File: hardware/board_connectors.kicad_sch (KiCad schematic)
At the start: 15 parts, among them J1 AudioJack2_Ground, J1 Conn_02x10_Odd_Even, J2 Conn_02x10_Odd_Even, J3 Conn_02x10_Odd_Even, J5 AudioJack2_Ground, J6 Conn_02x03_Odd_Even, J7 AudioJack2_Ground, J7 USB_B_Micro

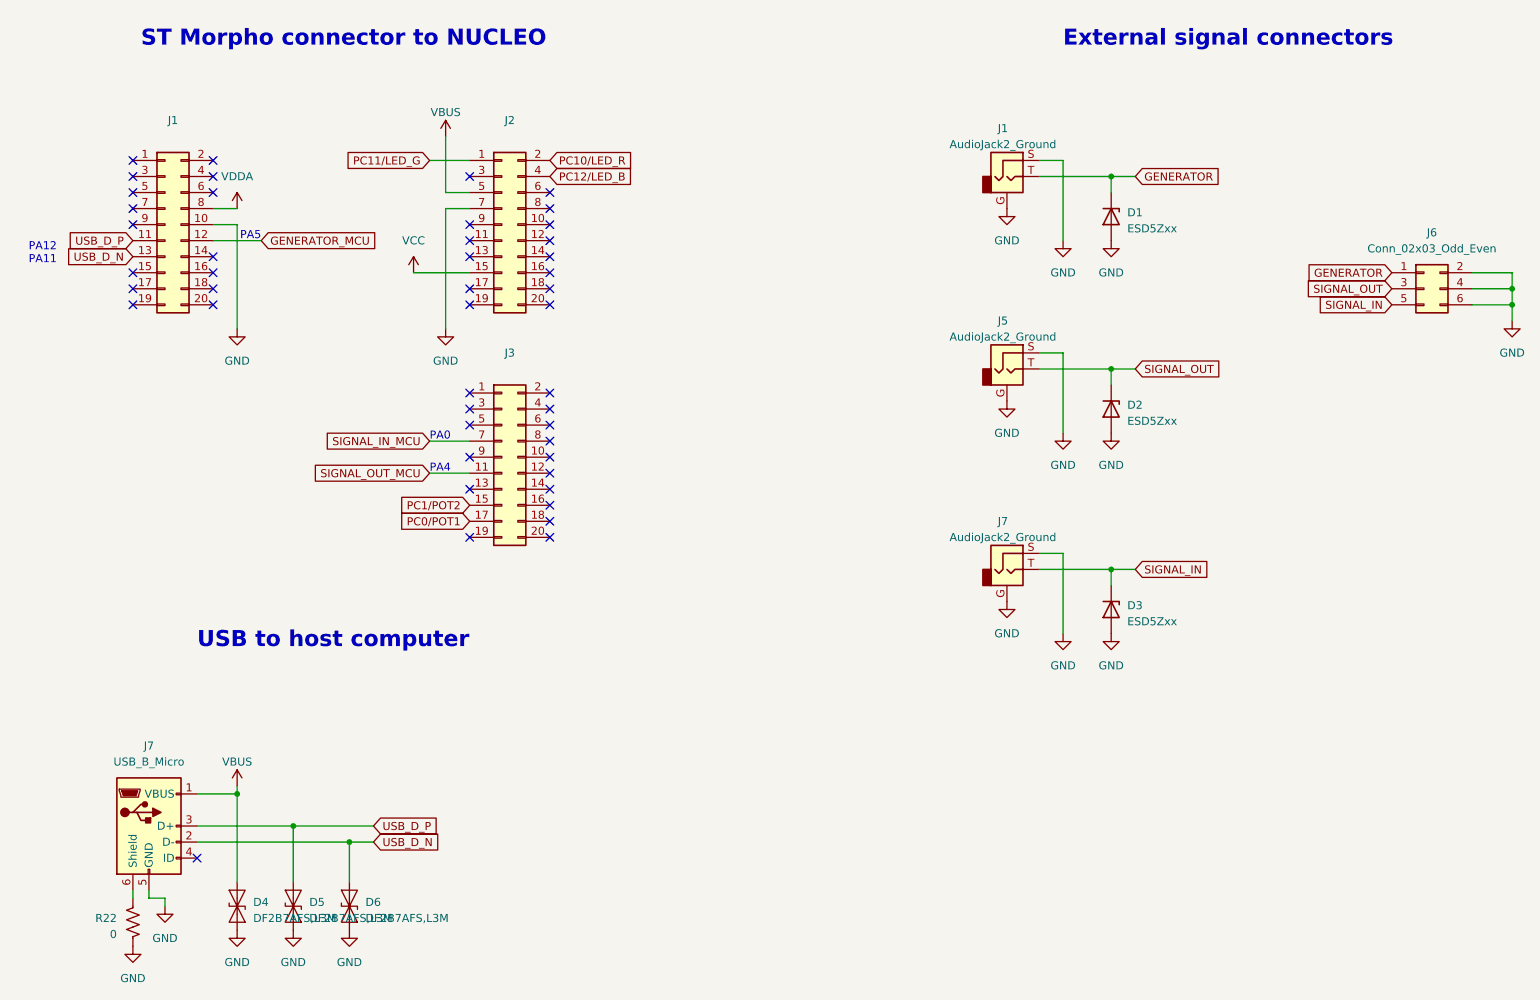
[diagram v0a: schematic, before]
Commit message: finalize pcb design; add layout file
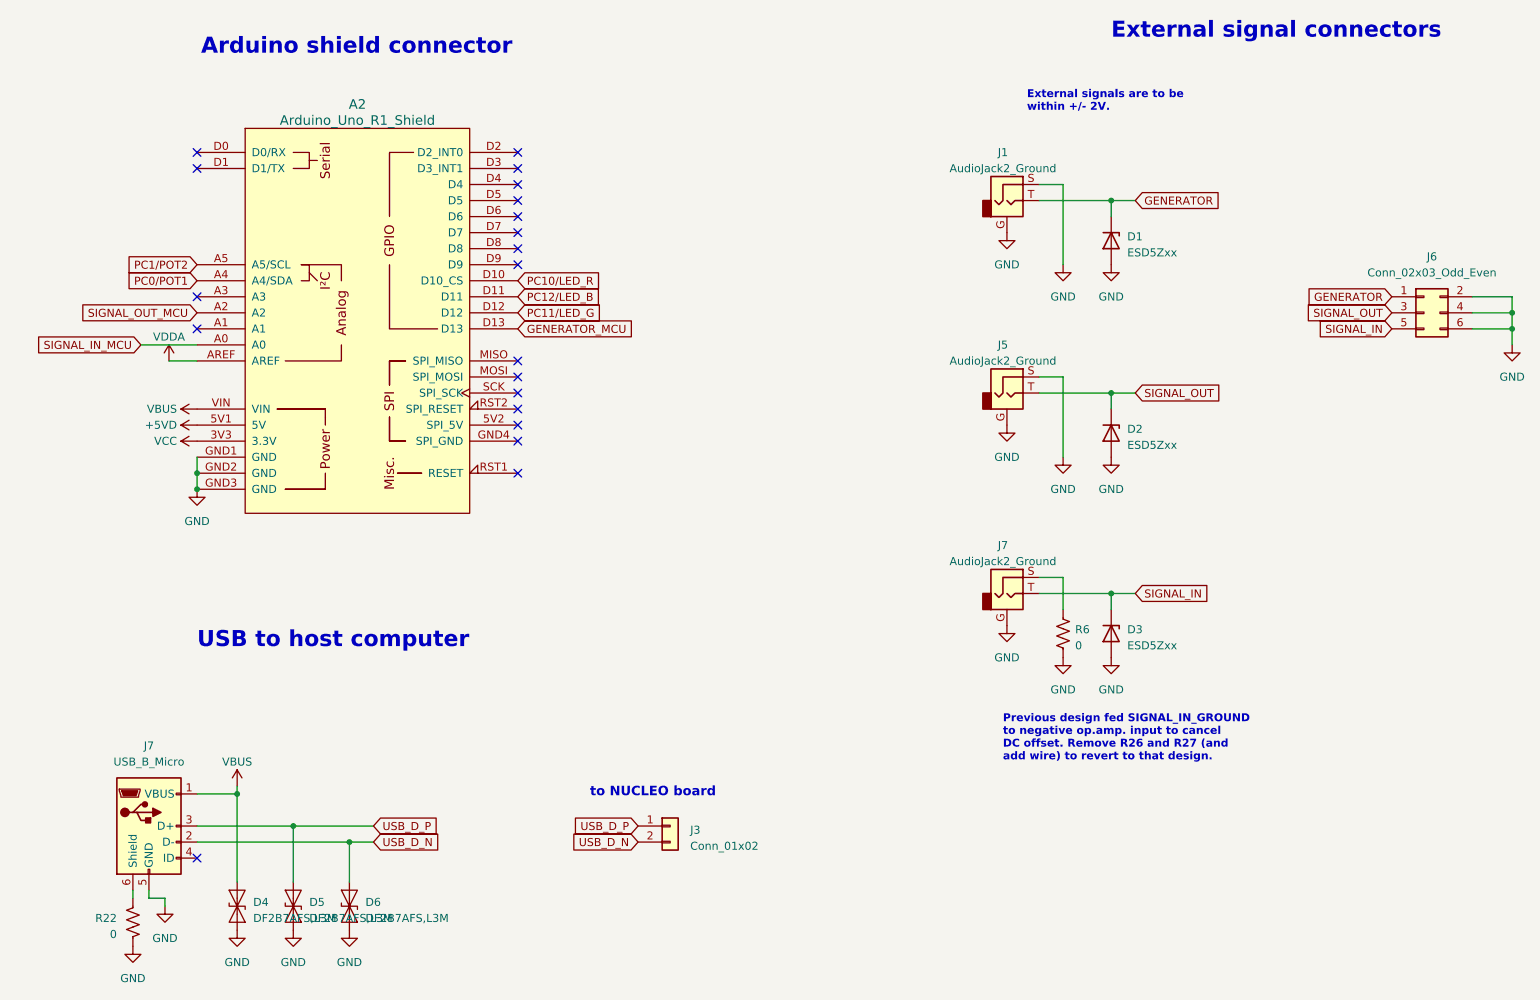
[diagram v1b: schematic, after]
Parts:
- removed J1, J2, J3: Conn_02x10_Odd_Even, Connector_PinHeader_2.54mm:PinHeader_2x10_P2.54mm_Vertical, symbol Connector_Generic:Conn_02x10_Odd_Even
- added A2: Arduino_Uno_R1_Shield, PCM_arduino-library:Arduino_Uno_R2_Shield, symbol PCM_arduino-library:Arduino_Uno_R1_Shield
- added J3: Conn_01x02, Connector_PinHeader_2.54mm:PinHeader_1x02_P2.54mm_Vertical, symbol Connector_Generic:Conn_01x02
- added R6: 0, Resistor_SMD:R_0603_1608Metric, symbol Device:R_US
- J6: footprint Connector_PinHeader_2.54mm:PinHeader_2x03_P2.54mm_Horizontal -> Connector_PinHeader_2.54mm:PinHeader_2x03_P2.54mm_Vertical; Part Number PH2RA-06-UA -> PH2-06-UA
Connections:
- net GENERATOR_MCU: now also A2.D13
- net GND: now also A2.GND1 (GND), A2.GND2 (GND), A2.GND3 (GND), R6.1; no longer J7.S
- net PC0/POT1: now also A2.A4 (A4/SDA)
- net PC10/LED_R: now also A2.D10 (D10_CS)
- net PC11/LED_G: now also A2.D12
- net PC12/LED_B: now also A2.D11
- net PC1/POT2: now also A2.A5 (A5/SCL)
- net SIGNAL_IN_MCU: now also A2.A0
- net SIGNAL_OUT_MCU: now also A2.A2
- net USB_D_N: now also J3.2 (Pin_2)
- net USB_D_P: now also J3.1 (Pin_1)
- net VBUS: now also A2.VIN
- net VCC: now also A2.3V3 (3.3V)
- net VDDA: now also A2.AREF
- new net: J7.S, R6.2
- new net +5VD: A2.5V1 (5V)
- no-connect marks 46 -> 20
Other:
- note added: "Arduino shield connector"
- note added: "External signals are to be within +/- 2V."
- note added: "Previous design fed SIGNAL_IN_GROUND to negative op.amp. input to cancel DC offset. Remove R26 and R27 (and add wire) to revert to that design."
- note added: "to NUCLEO board"
- note removed: "PA0"
- note removed: "PA12 PA11"
- note removed: "PA4"
- note removed: "PA5"
- note removed: "ST Morpho connector to NUCLEO"
- moved on the sheet: D1, D2, D3, J1, J5, J6, J7

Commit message: pcb design finalization
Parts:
- A2, J3: DNP (none) -> T
- D1, D2, D3: value ESD5Zxx -> ESD5Z2.5T1G; LCSC Part # (none) -> C475683
- D4, D5, D6: LCSC Part # (none) -> C1972965
- J1, J5, J7: LCSC Part # (none) -> C431535; Part Number SJ-3523-SMT-TR -> 2
- J6: LCSC Part # (none) -> C65114
- J7: LCSC Part # (none) -> C428496
- R22, R6: LCSC Part # (none) -> C21189
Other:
- title: Board and I/O connectors -> DSP PAW add-on board
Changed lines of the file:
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@@
   (paper "A4")
   (title_block
-    (title "Board and I/O connectors")
-    (date "2023-08-15")
+    (title "DSP PAW add-on board")
+    (date "2023-08-18")
     (company "bitgloo")
     (comment 1 "Released under the CERN Open Hardware Licence Version 2 - Strongly Reciprocal")
@@
       (effects (font (size 1.27 1.27)) hide)
     )
+    (property "DNP" "" (at 55.88 166.37 0)
+      (effects (font (size 1.27 1.27)) hide)
+    )
+    (property "LCSC Part #" "C1972965" (at 55.88 166.37 0)
+      (effects (font (size 1.27 1.27)) hide)
+    )
     (pin "1")
     (pin "2")
@@
     (property "Datasheet" "https://startingelectronics.org/articles/arduino/uno-r3-r2-differences/" (at 74.93 107.95 0)
       (effects (font (size 1.524 1.524)) hide)
+    )
+    (property "DNP" "T" (at 74.93 73.66 0)
+      (effects (font (size 1.27 1.27)) hide)
+    )
+    (property "LCSC Part #" "" (at 74.93 73.66 0)
+      (effects (font (size 1.27 1.27)) hide)
     )
     (pin "3V3")
@@
       (effects (font (size 1.27 1.27)) hide)
     )
+    (property "DNP" "" (at 64.77 166.37 0)
+      (effects (font (size 1.27 1.27)) hide)
+    )
+    (property "LCSC Part #" "C1972965" (at 64.77 166.37 0)
+      (effects (font (size 1.27 1.27)) hide)
+    )
     (pin "1")
     (pin "2")
@@
       (effects (font (size 1.27 1.27)) hide)
     )
-    (property "Part Number" "SJ-3523-SMT-TR" (at 177.8 85.09 0)
+    (property "Part Number" "2" (at 177.8 85.09 0)
+      (effects (font (size 1.27 1.27)) hide)
+    )
+    (property "DNP" "" (at 177.8 85.09 0)
+      (effects (font (size 1.27 1.27)) hide)
+    )
+    (property "LCSC Part #" "C431535" (at 177.8 85.09 0)
       (effects (font (size 1.27 1.27)) hide)
     )
@@
       (effects (font (size 1.27 1.27)) (justify left))
     )
-    (property "Value" "ESD5Zxx" (at 196.85 125.095 90)
+    (property "Value" "ESD5Z2.5T1G" (at 196.85 125.095 90)
       (effects (font (size 1.27 1.27)) (justify left))
     )
@@
     )
     (property "Part Number" "ESD5Z2.5T1G" (at 194.31 123.19 0)
+      (effects (font (size 1.27 1.27)) hide)
+    )
+    (property "DNP" "" (at 194.31 123.19 0)
+      (effects (font (size 1.27 1.27)) hide)
+    )
+    (property "LCSC Part #" "C475683" (at 194.31 123.19 0)
       (effects (font (size 1.27 1.27)) hide)
     )
@@
       (effects (font (size 1.27 1.27)) (justify left))
     )
-    (property "Value" "ESD5Zxx" (at 196.85 62.865 90)
+    (property "Value" "ESD5Z2.5T1G" (at 196.85 62.865 90)
       (effects (font (size 1.27 1.27)) (justify left))
     )
@@
     )
     (property "Part Number" "ESD5Z2.5T1G" (at 194.31 60.96 0)
+      (effects (font (size 1.27 1.27)) hide)
+    )
+    (property "DNP" "" (at 194.31 60.96 0)
+      (effects (font (size 1.27 1.27)) hide)
+    )
+    (property "LCSC Part #" "C475683" (at 194.31 60.96 0)
       (effects (font (size 1.27 1.27)) hide)
     )
@@
       (effects (font (size 1.27 1.27)) (justify left))
     )
-    (property "Value" "ESD5Zxx" (at 196.85 93.345 90)
+    (property "Value" "ESD5Z2.5T1G" (at 196.85 93.345 90)
       (effects (font (size 1.27 1.27)) (justify left))
     )
@@
       (effects (font (size 1.27 1.27)) hide)
     )
+    (property "DNP" "" (at 194.31 91.44 0)
+      (effects (font (size 1.27 1.27)) hide)
+    )
+    (property "LCSC Part #" "C475683" (at 194.31 91.44 0)
+      (effects (font (size 1.27 1.27)) hide)
+    )
     (pin "1")
     (pin "2")
@@
       (effects (font (size 1.27 1.27)) hide)
     )
-    (property "Part Number" "SJ-3523-SMT-TR" (at 177.8 54.61 0)
+    (property "Part Number" "2" (at 177.8 54.61 0)
+      (effects (font (size 1.27 1.27)) hide)
+    )
+    (property "DNP" "" (at 177.8 54.61 0)
+      (effects (font (size 1.27 1.27)) hide)
+    )
+    (property "LCSC Part #" "C431535" (at 177.8 54.61 0)
       (effects (font (size 1.27 1.27)) hide)
     )
@@
     )
     (property "Part Number" "10104110-0001LF" (at 41.91 153.67 0)
+      (effects (font (size 1.27 1.27)) hide)
+    )
+    (property "DNP" "" (at 41.91 153.67 0)
+      (effects (font (size 1.27 1.27)) hide)
+    )
+    (property "LCSC Part #" "C428496" (at 41.91 153.67 0)
       (effects (font (size 1.27 1.27)) hide)
     )
@@
       (effects (font (size 1.27 1.27)) hide)
     )
+    (property "DNP" "" (at 186.69 123.19 0)
+      (effects (font (size 1.27 1.27)) hide)
+    )
+    (property "LCSC Part #" "C21189" (at 186.69 123.19 0)
+      (effects (font (size 1.27 1.27)) hide)
+    )
     (pin "1")
     (pin "2")
@@
       (effects (font (size 1.27 1.27)) hide)
     )
-    (property "Part Number" "SJ-3523-SMT-TR" (at 177.8 116.84 0)
+    (property "Part Number" "2" (at 177.8 116.84 0)
+      (effects (font (size 1.27 1.27)) hide)
+    )
+    (property "DNP" "" (at 177.8 116.84 0)
+      (effects (font (size 1.27 1.27)) hide)
+    )
+    (property "LCSC Part #" "C431535" (at 177.8 116.84 0)
       (effects (font (size 1.27 1.27)) hide)
     )
@@
       (effects (font (size 1.27 1.27)) hide)
     )
+    (property "DNP" "" (at 39.37 168.91 0)
+      (effects (font (size 1.27 1.27)) hide)
+    )
+    (property "LCSC Part #" "C21189" (at 39.37 168.91 0)
+      (effects (font (size 1.27 1.27)) hide)
+    )
     (pin "1")
     (pin "2")
@@
       (effects (font (size 1.27 1.27)) hide)
     )
+    (property "DNP" "T" (at 124.46 153.67 0)
+      (effects (font (size 1.27 1.27)) hide)
+    )
+    (property "LCSC Part #" "" (at 124.46 153.67 0)
+      (effects (font (size 1.27 1.27)) hide)
+    )
     (pin "1")
     (pin "2")
@@
       (effects (font (size 1.27 1.27)) hide)
     )
+    (property "DNP" "" (at 73.66 166.37 0)
+      (effects (font (size 1.27 1.27)) hide)
+    )
+    (property "LCSC Part #" "C1972965" (at 73.66 166.37 0)
+      (effects (font (size 1.27 1.27)) hide)
+    )
     (pin "1")
     (pin "2")
@@
       (effects (font (size 1.27 1.27)) hide)
     )
+    (property "DNP" "" (at 243.84 72.39 0)
+      (effects (font (size 1.27 1.27)) hide)
+    )
+    (property "LCSC Part #" "C65114" (at 243.84 72.39 0)
+      (effects (font (size 1.27 1.27)) hide)
+    )
